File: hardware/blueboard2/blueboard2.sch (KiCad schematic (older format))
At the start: 106 parts, among them Q1 TRANSISTOR_NPN, Q2 TRANSISTOR_NPN, Q3 TRANSISTOR_NPN, SW1 SW_SPST

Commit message: round 2 of board design
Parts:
- removed BT1: BATTERY, ~, symbol BATTERY
- removed JP2: M07, symbol M07
- removed SW1: SW_SPST, symbol SW_SPST
- added C1: 10uF, Freetronics:CAP_ELECTRO_D4S1.8, symbol CAP
- added HC1: HC05, finn_kicad:HC05, symbol HC05
- added JP10, JP11, JP12, JP13, JP14, JP15, JP16, JP17, JP18, JP19, JP2, JP20, JP21, JP22, JP3, JP4, JP5, JP6, JPG1, JPG2, JPG3, JPG4, JPVIN1: M01, Freetronics:1X01, symbol M01
- added MOUNT1, MOUNT2, MOUNT3, MOUNT4, MOUNT5: M01, Wire_Pads:SolderWirePad_single_2mmDrill, symbol M01
- added R17: 10k, Resistors_ThroughHole:Resistor_Horizontal_RM10mm, symbol R
- added SW2: SW_PUSHBUTTON, Freetronics:1X02, symbol SW_PUSHBUTTON
- added U?: BUZZER, symbol BUZZER
- D1, D10, D11, D12, D13, D14, D15, D16, D2, D3, D4, D5, D6, D7, D8, D9: footprint ~ -> Freetronics:LED-5MM
- JP1: footprint (none) -> Freetronics:1X01
- LDR1: renamed from R66; value RES_PHOTO_LDR -> LDR; footprint (none) -> Resistors_ThroughHole:Resistor_Horizontal_RM15mm
- LDR10: renamed from R84; value RES_PHOTO_LDR -> LDR; footprint (none) -> Resistors_ThroughHole:Resistor_Horizontal_RM15mm
- LDR11: renamed from R86; value RES_PHOTO_LDR -> LDR; footprint (none) -> Resistors_ThroughHole:Resistor_Horizontal_RM15mm
- LDR12: renamed from R88; value RES_PHOTO_LDR -> LDR; footprint (none) -> Resistors_ThroughHole:Resistor_Horizontal_RM15mm
- LDR13: renamed from R90; value RES_PHOTO_LDR -> LDR; footprint (none) -> Resistors_ThroughHole:Resistor_Horizontal_RM15mm
- LDR14: renamed from R92; value RES_PHOTO_LDR -> LDR; footprint (none) -> Resistors_ThroughHole:Resistor_Horizontal_RM15mm
- LDR15: renamed from R94; value RES_PHOTO_LDR -> LDR; footprint (none) -> Resistors_ThroughHole:Resistor_Horizontal_RM15mm
- LDR16: renamed from R96; value RES_PHOTO_LDR -> LDR; footprint (none) -> Resistors_ThroughHole:Resistor_Horizontal_RM15mm
- LDR2: renamed from R68; value RES_PHOTO_LDR -> LDR; footprint (none) -> Resistors_ThroughHole:Resistor_Horizontal_RM15mm
- LDR3: renamed from R70; value RES_PHOTO_LDR -> LDR; footprint (none) -> Resistors_ThroughHole:Resistor_Horizontal_RM15mm
- LDR4: renamed from R72; value RES_PHOTO_LDR -> LDR; footprint (none) -> Resistors_ThroughHole:Resistor_Horizontal_RM15mm
- LDR5: renamed from R74; value RES_PHOTO_LDR -> LDR; footprint (none) -> Resistors_ThroughHole:Resistor_Horizontal_RM15mm
- LDR6: renamed from R76; value RES_PHOTO_LDR -> LDR; footprint (none) -> Resistors_ThroughHole:Resistor_Horizontal_RM15mm
- LDR7: renamed from R78; value RES_PHOTO_LDR -> LDR; footprint (none) -> Resistors_ThroughHole:Resistor_Horizontal_RM15mm
- LDR8: renamed from R80; value RES_PHOTO_LDR -> LDR; footprint (none) -> Resistors_ThroughHole:Resistor_Horizontal_RM15mm
- LDR9: renamed from R82; value RES_PHOTO_LDR -> LDR; footprint (none) -> Resistors_ThroughHole:Resistor_Horizontal_RM15mm
- LED1, LED10, LED11, LED12, LED13, LED14, LED15, LED16, LED2, LED3, LED4, LED5, LED6, LED7, LED8, LED9: footprint (none) -> finn_kicad:LED-RGB-comA-5MM
- Q1, Q2, Q3: footprint (none) -> finn_kicad:EBC-transistor-NPN
- R1, R10, R11, R12, R13, R14, R15, R16, R2, R3, R4, R5, R6, R7, R8, R9: value 220 -> 470; footprint (none) -> Resistors_ThroughHole:Resistor_Horizontal_RM10mm
- R49, R50, R51, R52, R53, R54, R55, R56, R57, R58, R59, R60, R61, R62, R63, R64, R65, R67, R69, R71, R73, R75, R77, R79, R81, R83, R85, R87, R89, R91, R93, R95, R97: footprint ~ -> Resistors_ThroughHole:Resistor_Horizontal_RM10mm
- R98: value R -> 2.2k; footprint ~ -> Resistors_ThroughHole:Resistor_Horizontal_RM10mm
- SHIELD1: footprint FT:ARDUINO_MEGA_SHIELD -> Freetronics:ARDUINO_MEGA_SHIELD
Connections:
- net labels removed: VCC
- wire segments 384 -> 368
- no-connect marks 0 -> 20
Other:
- moved on the sheet: R97, R98

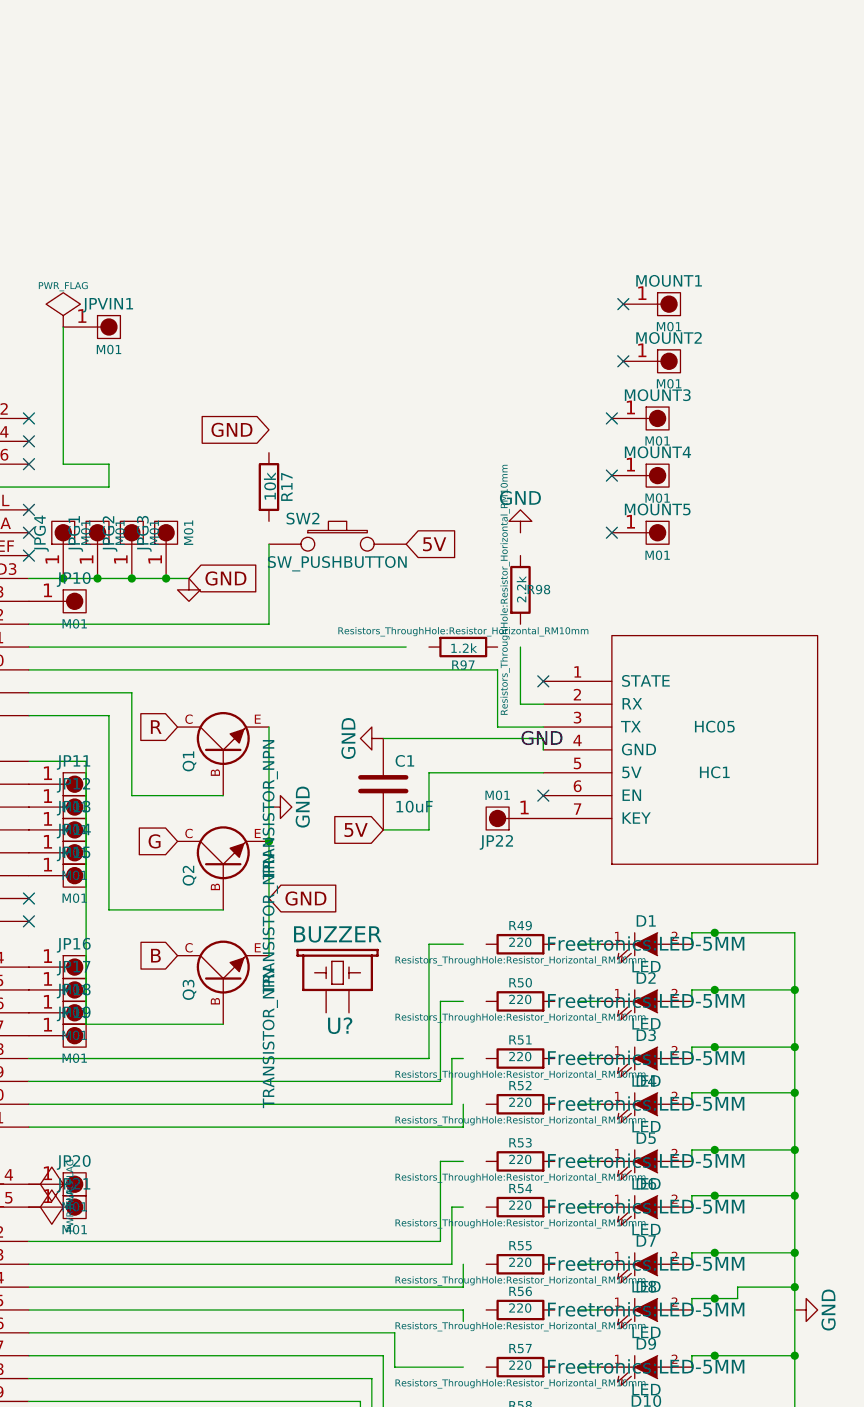
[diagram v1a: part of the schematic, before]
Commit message: state when board sent to manufacture
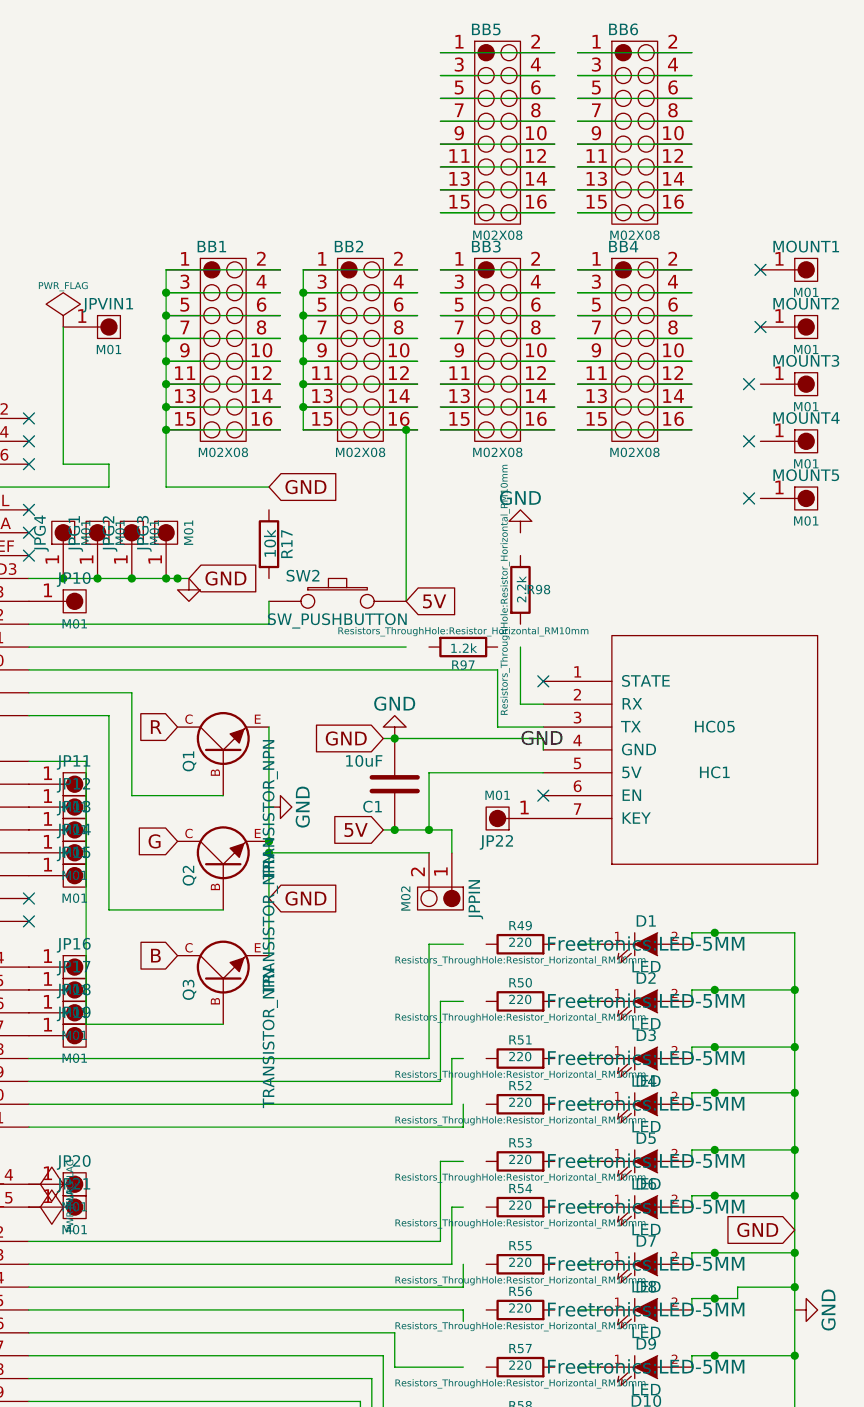
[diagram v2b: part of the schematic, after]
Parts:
- removed U?: BUZZER, symbol BUZZER
- added BB1, BB2, BB3, BB4, BB5, BB6: M02X08, Freetronics:2X8, symbol M02X08
- added JPPIN: M02, symbol M02
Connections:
- wire segments 368 -> 422
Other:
- moved on the sheet: C1, MOUNT1, MOUNT2, MOUNT3, MOUNT4, MOUNT5, R17, SW2

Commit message: lots of changes
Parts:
- D1, D10, D11, D12, D13, D14, D15, D16, D2, D3, D4, D5, D6, D7, D8, D9: footprint Freetronics:LED-5MM -> finn_kicad:LED-5MM
- JPPIN1: renamed from JPPIN; footprint (none) -> Freetronics:1X02
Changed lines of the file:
@@
 F 0 "D3" H 10450 4200 50  0000 C CNN
 F 1 "LED" H 10450 4000 50  0000 C CNN
-F 2 "Freetronics:LED-5MM" H 10450 4100 60  0000 C CNN
+F 2 "finn_kicad:LED-5MM" H 10450 4100 60  0000 C CNN
 F 3 "~" H 10450 4100 60  0000 C CNN
 	1    10450 4100
@@
 F 0 "D2" H 10450 3950 50  0000 C CNN
 F 1 "LED" H 10450 3750 50  0000 C CNN
-F 2 "Freetronics:LED-5MM" H 10450 3850 60  0000 C CNN
+F 2 "finn_kicad:LED-5MM" H 10450 3850 60  0000 C CNN
 F 3 "~" H 10450 3850 60  0000 C CNN
 	1    10450 3850
@@
 F 0 "D5" H 10450 4650 50  0000 C CNN
 F 1 "LED" H 10450 4450 50  0000 C CNN
-F 2 "Freetronics:LED-5MM" H 10450 4550 60  0000 C CNN
+F 2 "finn_kicad:LED-5MM" H 10450 4550 60  0000 C CNN
 F 3 "~" H 10450 4550 60  0000 C CNN
 	1    10450 4550
@@
 F 0 "D4" H 10450 4400 50  0000 C CNN
 F 1 "LED" H 10450 4200 50  0000 C CNN
-F 2 "Freetronics:LED-5MM" H 10450 4300 60  0000 C CNN
+F 2 "finn_kicad:LED-5MM" H 10450 4300 60  0000 C CNN
 F 3 "~" H 10450 4300 60  0000 C CNN
 	1    10450 4300
@@
 F 0 "D7" H 10450 5100 50  0000 C CNN
 F 1 "LED" H 10450 4900 50  0000 C CNN
-F 2 "Freetronics:LED-5MM" H 10450 5000 60  0000 C CNN
+F 2 "finn_kicad:LED-5MM" H 10450 5000 60  0000 C CNN
 F 3 "~" H 10450 5000 60  0000 C CNN
 	1    10450 5000
@@
 F 0 "D6" H 10450 4850 50  0000 C CNN
 F 1 "LED" H 10450 4650 50  0000 C CNN
-F 2 "Freetronics:LED-5MM" H 10450 4750 60  0000 C CNN
+F 2 "finn_kicad:LED-5MM" H 10450 4750 60  0000 C CNN
 F 3 "~" H 10450 4750 60  0000 C CNN
 	1    10450 4750
@@
 F 0 "D9" H 10450 5550 50  0000 C CNN
 F 1 "LED" H 10450 5350 50  0000 C CNN
-F 2 "Freetronics:LED-5MM" H 10450 5450 60  0000 C CNN
+F 2 "finn_kicad:LED-5MM" H 10450 5450 60  0000 C CNN
 F 3 "~" H 10450 5450 60  0000 C CNN
 	1    10450 5450
@@
 F 0 "D8" H 10450 5300 50  0000 C CNN
 F 1 "LED" H 10450 5100 50  0000 C CNN
-F 2 "Freetronics:LED-5MM" H 10450 5200 60  0000 C CNN
+F 2 "finn_kicad:LED-5MM" H 10450 5200 60  0000 C CNN
 F 3 "~" H 10450 5200 60  0000 C CNN
 	1    10450 5200
@@
 F 0 "D11" H 10450 6050 50  0000 C CNN
 F 1 "LED" H 10450 5850 50  0000 C CNN
-F 2 "Freetronics:LED-5MM" H 10450 5950 60  0000 C CNN
+F 2 "finn_kicad:LED-5MM" H 10450 5950 60  0000 C CNN
 F 3 "~" H 10450 5950 60  0000 C CNN
 	1    10450 5950
@@
 F 0 "D10" H 10450 5800 50  0000 C CNN
 F 1 "LED" H 10450 5600 50  0000 C CNN
-F 2 "Freetronics:LED-5MM" H 10450 5700 60  0000 C CNN
+F 2 "finn_kicad:LED-5MM" H 10450 5700 60  0000 C CNN
 F 3 "~" H 10450 5700 60  0000 C CNN
 	1    10450 5700
@@
 F 0 "D13" H 10450 6500 50  0000 C CNN
 F 1 "LED" H 10450 6300 50  0000 C CNN
-F 2 "Freetronics:LED-5MM" H 10450 6400 60  0000 C CNN
+F 2 "finn_kicad:LED-5MM" H 10450 6400 60  0000 C CNN
 F 3 "~" H 10450 6400 60  0000 C CNN
 	1    10450 6400
@@
 F 0 "D12" H 10450 6250 50  0000 C CNN
 F 1 "LED" H 10450 6050 50  0000 C CNN
-F 2 "Freetronics:LED-5MM" H 10450 6150 60  0000 C CNN
+F 2 "finn_kicad:LED-5MM" H 10450 6150 60  0000 C CNN
 F 3 "~" H 10450 6150 60  0000 C CNN
 	1    10450 6150
@@
 F 0 "D15" H 10450 6950 50  0000 C CNN
 F 1 "LED" H 10450 6750 50  0000 C CNN
-F 2 "Freetronics:LED-5MM" H 10450 6850 60  0000 C CNN
+F 2 "finn_kicad:LED-5MM" H 10450 6850 60  0000 C CNN
 F 3 "~" H 10450 6850 60  0000 C CNN
 	1    10450 6850
@@
 F 0 "D14" H 10450 6700 50  0000 C CNN
 F 1 "LED" H 10450 6500 50  0000 C CNN
-F 2 "Freetronics:LED-5MM" H 10450 6600 60  0000 C CNN
+F 2 "finn_kicad:LED-5MM" H 10450 6600 60  0000 C CNN
 F 3 "~" H 10450 6600 60  0000 C CNN
 	1    10450 6600
@@
 F 0 "D1" H 10450 3700 50  0000 C CNN
 F 1 "LED" H 10450 3500 50  0000 C CNN
-F 2 "Freetronics:LED-5MM" H 10450 3600 60  0000 C CNN
+F 2 "finn_kicad:LED-5MM" H 10450 3600 60  0000 C CNN
 F 3 "~" H 10450 3600 60  0000 C CNN
 	1    10450 3600
@@
 F 0 "D16" H 10450 7150 50  0000 C CNN
 F 1 "LED" H 10450 6950 50  0000 C CNN
-F 2 "Freetronics:LED-5MM" H 10450 7050 60  0000 C CNN
+F 2 "finn_kicad:LED-5MM" H 10450 7050 60  0000 C CNN
 F 3 "~" H 10450 7050 60  0000 C CNN
 	1    10450 7050
@@
 $EndComp
 $Comp
-L M02 JPPIN
+L M02 JPPIN1
 U 1 1 550D02A5
 P 9600 3500
-F 0 "JPPIN" H 9500 3600 50  0000 C CNN
+F 0 "JPPIN1" H 9500 3600 50  0000 C CNN
 F 1 "M02" H 9500 3300 40  0000 C CNN
-F 2 "" H 9600 3500 60  0000 C CNN
+F 2 "Freetronics:1X02" H 9600 3500 60  0001 C CNN
 F 3 "" H 9600 3500 60  0000 C CNN
 	1    9600 3500
